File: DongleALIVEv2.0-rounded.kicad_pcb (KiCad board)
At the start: 2 copper layers, 45 x 55 mm, 77 parts, among them J1 C-OBD-II-16M, J2 Conn_01x05_Socket, J3 Conn_01x05_Socket, J4 USB_B_Micro, Q1 IRF5305S, Q2 SS8050-G, Q3 SS8050-G, SW1 SW_Push, SW2 SW_Push, SW3 SW_SPDT_321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

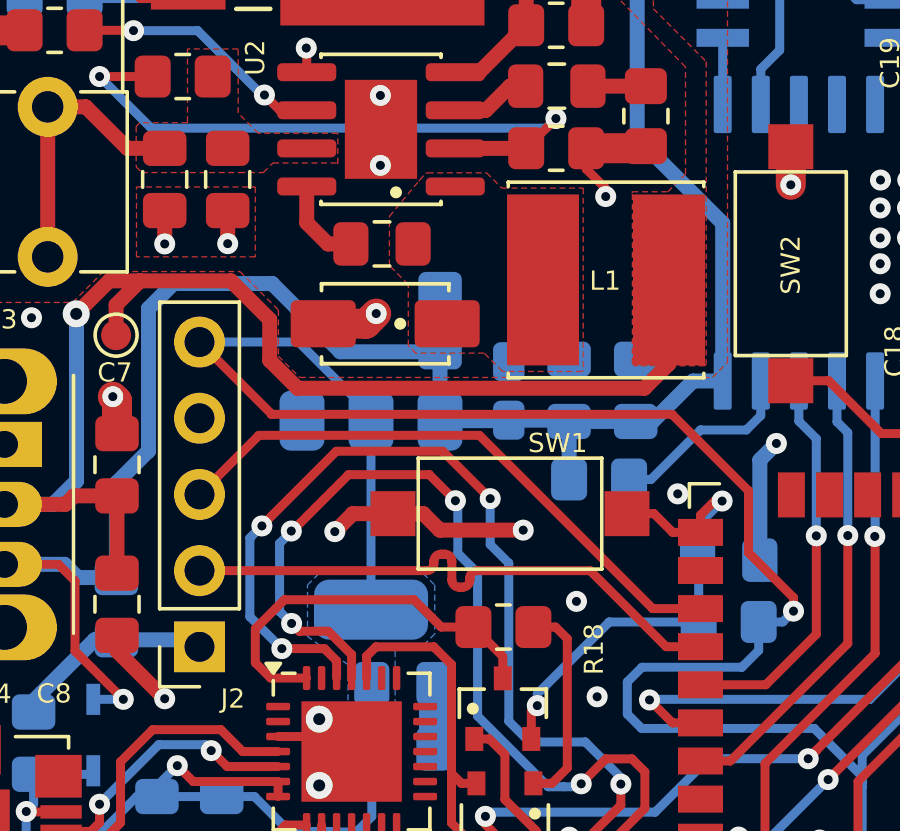
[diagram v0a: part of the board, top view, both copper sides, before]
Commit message: Fix CP2102 connection
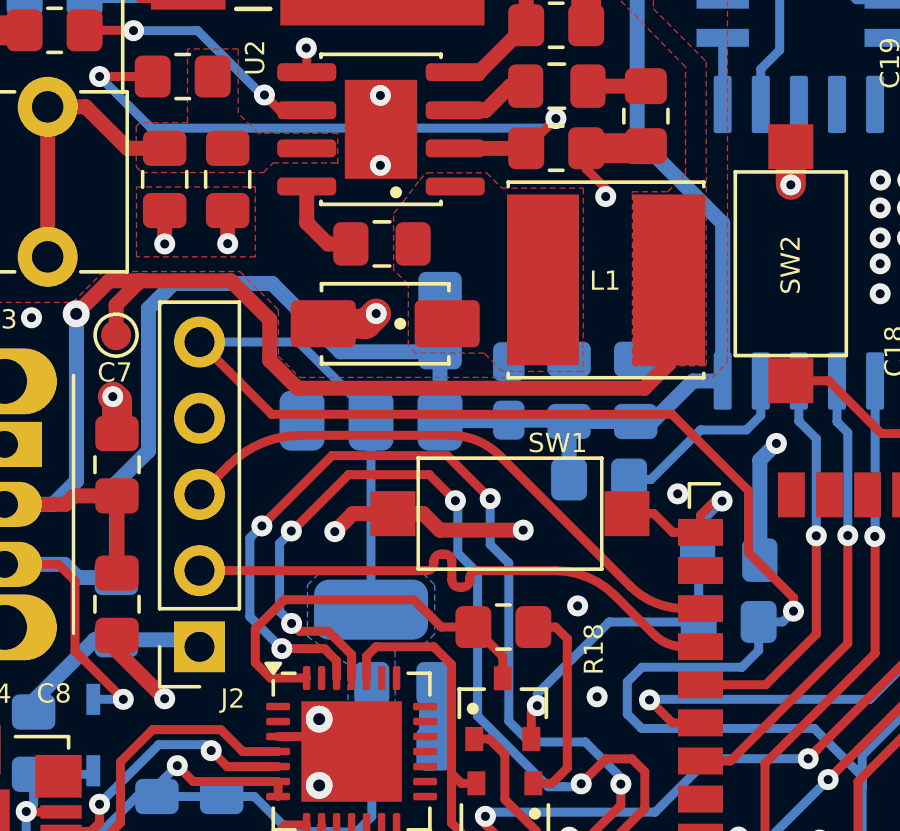
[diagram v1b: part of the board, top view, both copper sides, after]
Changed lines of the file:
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@@
 	)
 	(via
-		(at 136.29 103.61)
+		(at 136.33 103.76)
 		(size 0.7)
 		(drill 0.3)
@@
 	)
 	(segment
-		(start 133.055 98.075)
-		(end 125.705 98.075)
+		(start 132.096539 98.075)
+		(end 127.098 98.075)
 		(width 0.3)
 		(layer "F.Cu")
@@
 	)
 	(segment
-		(start 123.735 100.045)
+		(start 123.73 100.045)
 		(end 123.725 100.045)
 		(width 0.3)
@@
 	)
 	(segment
-		(start 140.425 103.85)
-		(end 138.83 103.85)
+		(start 139.892044 103.85)
+		(end 140.425 103.85)
 		(width 0.3)
 		(layer "F.Cu")
@@
 	)
 	(segment
-		(start 138.83 103.85)
-		(end 133.055 98.075)
+		(start 133.732734 98.752734)
+		(end 138.079021 103.099021)
 		(width 0.3)
 		(layer "F.Cu")
@@
 	)
 	(segment
-		(start 125.705 98.075)
-		(end 123.735 100.045)
+		(start 123.738535 100.041464)
+		(end 124.72 99.06)
+		(width 0.3)
+		(layer "F.Cu")
+		(net 32)
+	)
+	(arc
+		(start 123.738535 100.041464)
+		(mid 123.734619 100.044081)
+		(end 123.73 100.045)
+		(width 0.3)
+		(layer "F.Cu")
+		(net 32)
+	)
+	(arc
+		(start 127.098 98.075)
+		(mid 125.811035 98.330993)
+		(end 124.72 99.06)
+		(width 0.3)
+		(layer "F.Cu")
+		(net 32)
+	)
+	(arc
+		(start 133.732734 98.752734)
+		(mid 132.982041 98.251137)
+		(end 132.096539 98.075)
+		(width 0.3)
+		(layer "F.Cu")
+		(net 32)
+	)
+	(arc
+		(start 138.079021 103.099021)
+		(mid 138.910843 103.654827)
+		(end 139.892044 103.85)
 		(width 0.3)
 		(layer "F.Cu")
@@
 	)
 	(segment
-		(start 132.136989 102.895)
-		(end 132.136989 102.275)
+		(start 132.136989 102.275)
+		(end 132.136989 102.895)
 		(width 0.3)
 		(layer "F.Cu")
@@
 	)
 	(segment
-		(start 132.496989 103.135)
-		(end 132.376989 103.135)
+		(start 132.376989 103.135)
+		(end 132.496989 103.135)
 		(width 0.3)
 		(layer "F.Cu")
@@
 	)
 	(segment
-		(start 140.425 105.12)
-		(end 139.28 105.12)
+		(start 139.8525 105.12)
+		(end 140.425 105.12)
 		(width 0.3)
 		(layer "F.Cu")
@@
 	)
 	(segment
-		(start 139.28 105.12)
-		(end 136.745 102.585)
+		(start 138.875181 104.715181)
+		(end 137.573021 103.413021)
 		(width 0.3)
 		(layer "F.Cu")
@@
 	)
 	(segment
-		(start 131.536989 102.275)
-		(end 131.536989 102.345)
+		(start 131.536989 102.345)
+		(end 131.536989 102.275)
 		(width 0.3)
 		(layer "F.Cu")
@@
 	)
 	(segment
-		(start 131.896989 102.035)
-		(end 131.776989 102.035)
+		(start 131.776989 102.035)
+		(end 131.896989 102.035)
 		(width 0.3)
 		(layer "F.Cu")
@@
 	)
 	(segment
-		(start 136.745 102.585)
+		(start 135.574001 102.585)
 		(end 132.976989 102.585)
 		(width 0.3)
@@
 	)
 	(segment
-		(start 132.736989 102.825)
-		(end 132.736989 102.895)
+		(start 132.736989 102.895)
+		(end 132.736989 102.825)
 		(width 0.3)
 		(layer "F.Cu")
@@
 	)
 	(arc
+		(start 138.875181 104.715181)
+		(mid 139.323578 105.01479)
+		(end 139.8525 105.12)
+		(width 0.3)
+		(layer "F.Cu")
+		(net 33)
+	)
+	(arc
 		(start 132.136989 102.275)
 		(mid 132.066695 102.105294)
@@
 	)
 	(arc
-		(start 132.376989 103.135)
+		(start 132.136989 102.895)
 		(mid 132.207283 103.064706)
-		(end 132.136989 102.895)
+		(end 132.376989 103.135)
+		(width 0.3)
+		(layer "F.Cu")
+		(net 33)
+	)
+	(arc
+		(start 137.573021 103.413021)
+		(mid 136.655863 102.800196)
+		(end 135.574001 102.585)
 		(width 0.3)
 		(layer "F.Cu")
@@
 	)
 	(segment
-		(start 131.835 98.605)
-		(end 133.415 100.185)
+		(start 136.7 111.47)
+		(end 136.05 111.47)
 		(width 0.3)
 		(layer "F.Cu")
@@
 	)
 	(segment
-		(start 136.7 111.47)
-		(end 136.05 111.47)
+		(start 125.805 101.085)
+		(end 128.14 98.75)
 		(width 0.3)
 		(layer "F.Cu")
@@
 	)
 	(segment
-		(start 125.805 101.095)
-		(end 125.805 101.085)
+		(start 128.295 105.592106)
+		(end 127.941447 105.238553)
 		(width 0.3)
 		(layer "F.Cu")
@@
 	)
 	(segment
-		(start 128.295 105.592106)
-		(end 127.941447 105.238553)
+		(start 125.805 101.095)
+		(end 125.805 101.085)
 		(width 0.3)
 		(layer "F.Cu")
@@
 	)
 	(segment
-		(start 128.285 98.605)
-		(end 131.835 98.605)
+		(start 131.98 98.75)
+		(end 133.415 100.185)
 		(width 0.3)
 		(layer "F.Cu")
@@
 	)
 	(segment
-		(start 125.805 101.085)
-		(end 128.285 98.605)
+		(start 128.14 98.75)
+		(end 131.98 98.75)
 		(width 0.3)
 		(layer "F.Cu")
@@
 		(polygon
 			(pts
-				(xy 130.055 90.775) (xy 131.037792 89.597792) (xy 131.063542 89.563542) (xy 131.265291 89.344709)
+				(xy 130.195 90.675555) (xy 130.52182 90.284083) (xy 131.063542 89.563542) (xy 131.265291 89.344709)
 				(xy 131.329783 89.325) (xy 133.295 89.325) (xy 133.805 89.835) (xy 136.515 89.835) (xy 136.515 95.905)
 				(xy 136.475 95.945) (xy 133.825 95.945) (xy 133.215 95.335) (xy 130.975 95.335) (xy 130.955 95.355)
-				(xy 130.685 95.085) (xy 130.685 93.045) (xy 130.055 92.415)
+				(xy 130.685 95.085) (xy 130.685 93.045) (xy 130.195 92.555)
 			)
 		)
